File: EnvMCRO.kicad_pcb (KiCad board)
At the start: 2 copper layers, 109.6 x 69.7 mm, 30 parts, among them U1 Pico

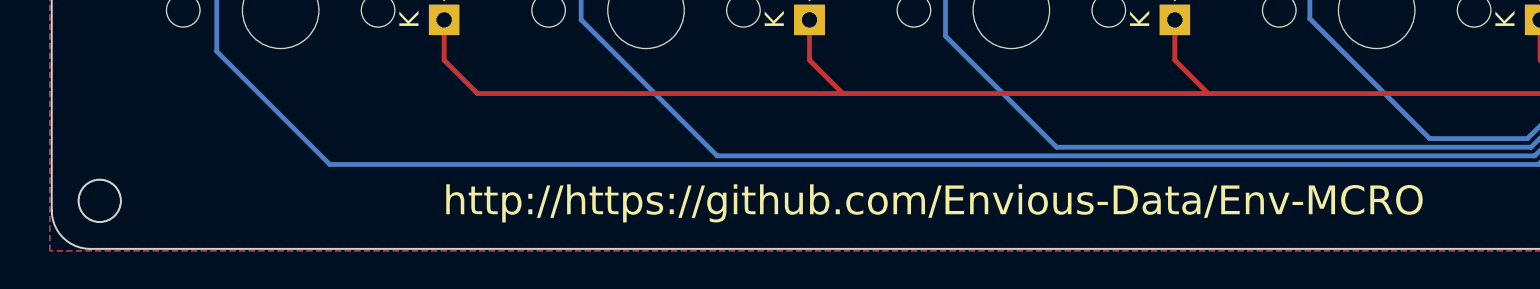
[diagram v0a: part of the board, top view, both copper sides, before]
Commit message: Fixed the error in the silkscreen
"http://https://" idk how I missed this
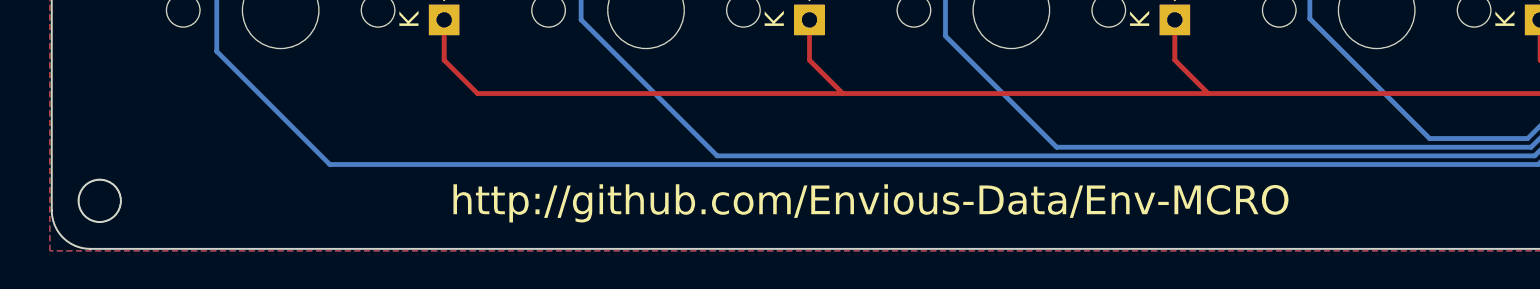
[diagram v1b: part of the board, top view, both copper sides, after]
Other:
- board text added: "http://github.com/Envious-Data/Env-MCRO"
- board text removed: "http://https://github.com/Envious-Data/Env-MCRO"

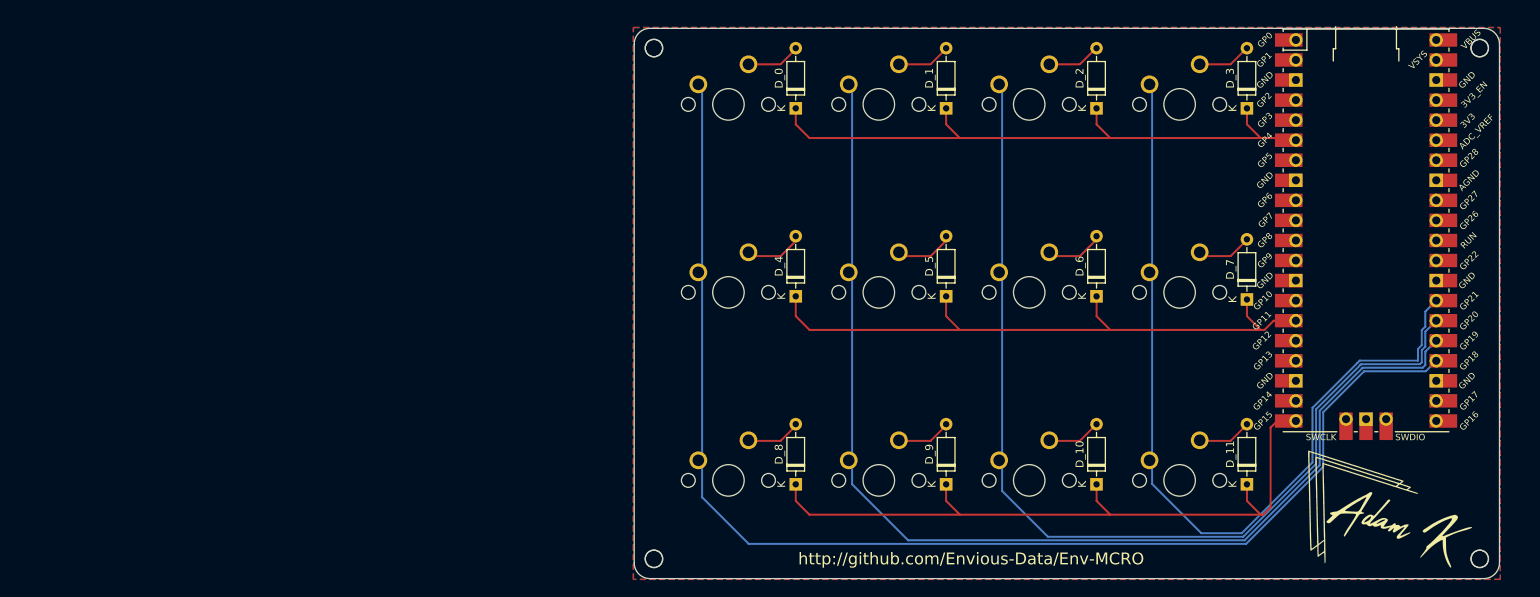
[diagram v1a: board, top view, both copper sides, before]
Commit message: Updated Gerber bits with new graphics design
and also correct format!
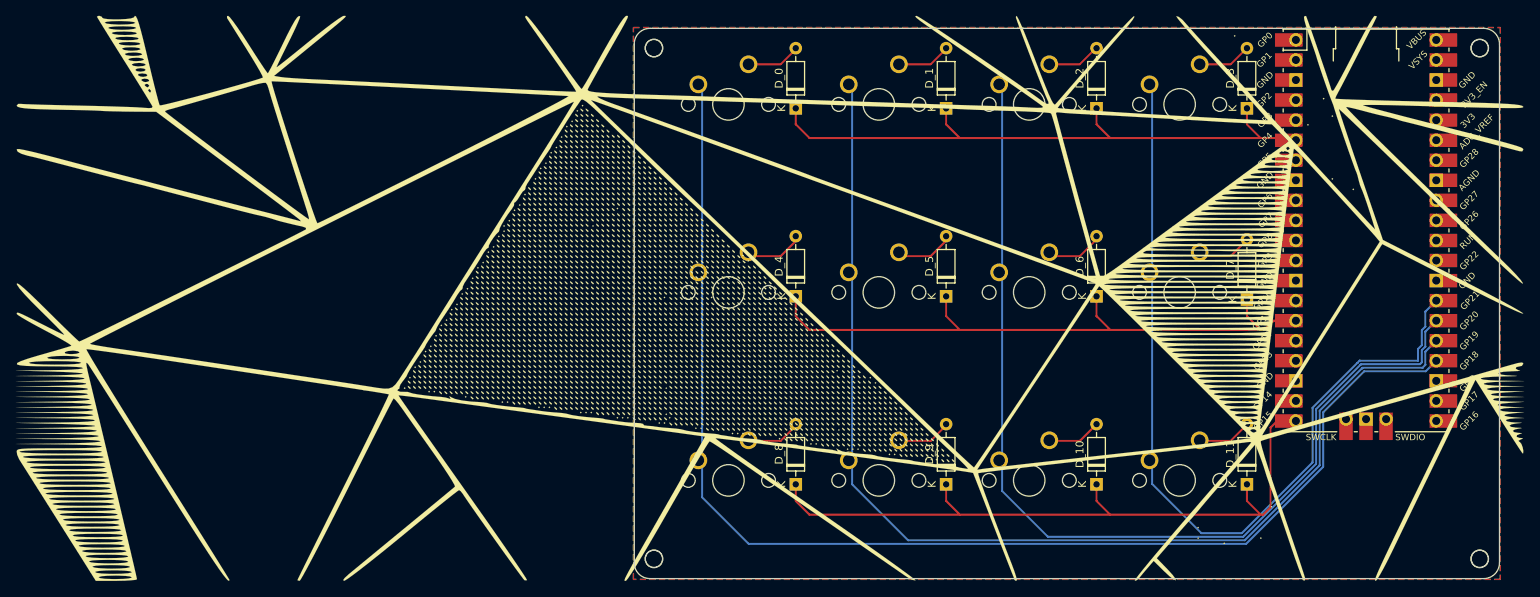
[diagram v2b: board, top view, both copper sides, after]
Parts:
- added G***: LOGO, Logo:test, F.Cu at (80.6, 73.0)
- added G***: LOGO, Logo:test, B.Cu at (78.5, 73.0)
- moved G*** 0.67 mm to (159.0, 99.4)
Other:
- board text removed: "http://github.com/Envious-Data/Env-MCRO"

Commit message: Updated graphics design on board
added the github URL back but now its shiny!
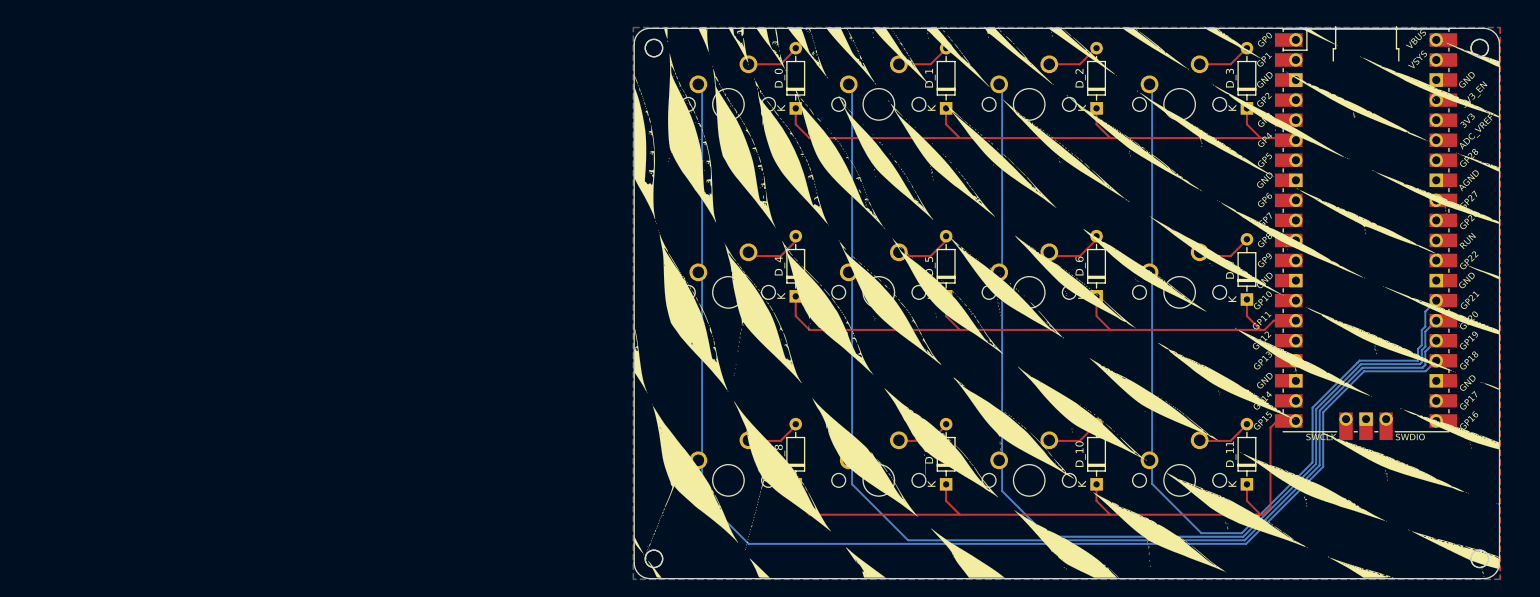
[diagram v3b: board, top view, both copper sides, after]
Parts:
- removed the G*** at (80.6, 73.0)
- removed the G*** at (78.5, 73.0)
- added G***: LOGO, Logo:test1, B.Cu at (118.0, 73.8)
- added G***: LOGO, Logo:test, F.Cu at (118.2, 73.5)
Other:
- board text added: "http://github.com/Envious-Data/Env-MCRO"
